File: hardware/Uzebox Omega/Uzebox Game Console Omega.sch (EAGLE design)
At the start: 81 parts, among them CON1 USBSERIALSMD, IC1 MCP1700, IC2 7805T, U5 DC IN, U6 23LC1024, X1 A/V

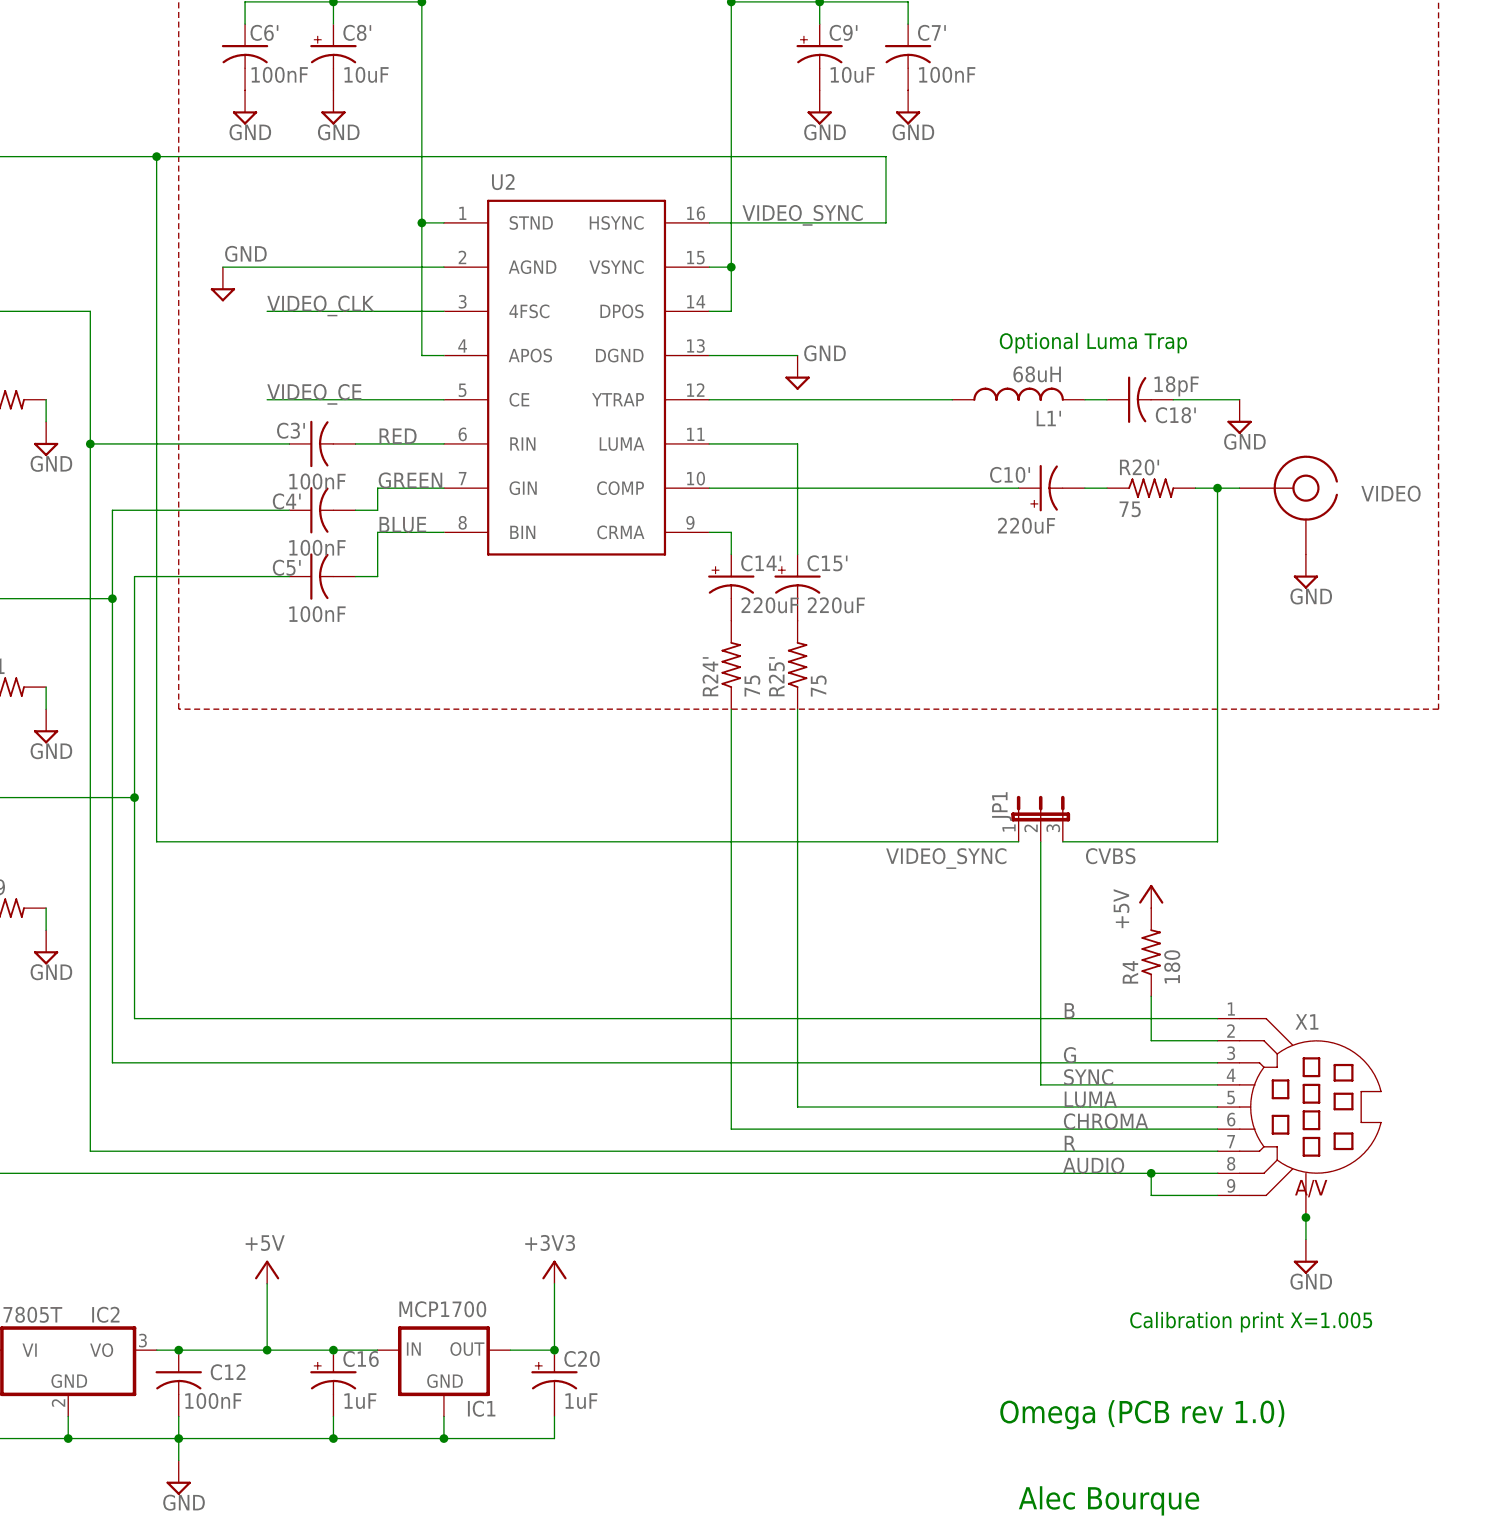
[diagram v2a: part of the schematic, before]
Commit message: Corrected pinout for Sega Megadrive cables
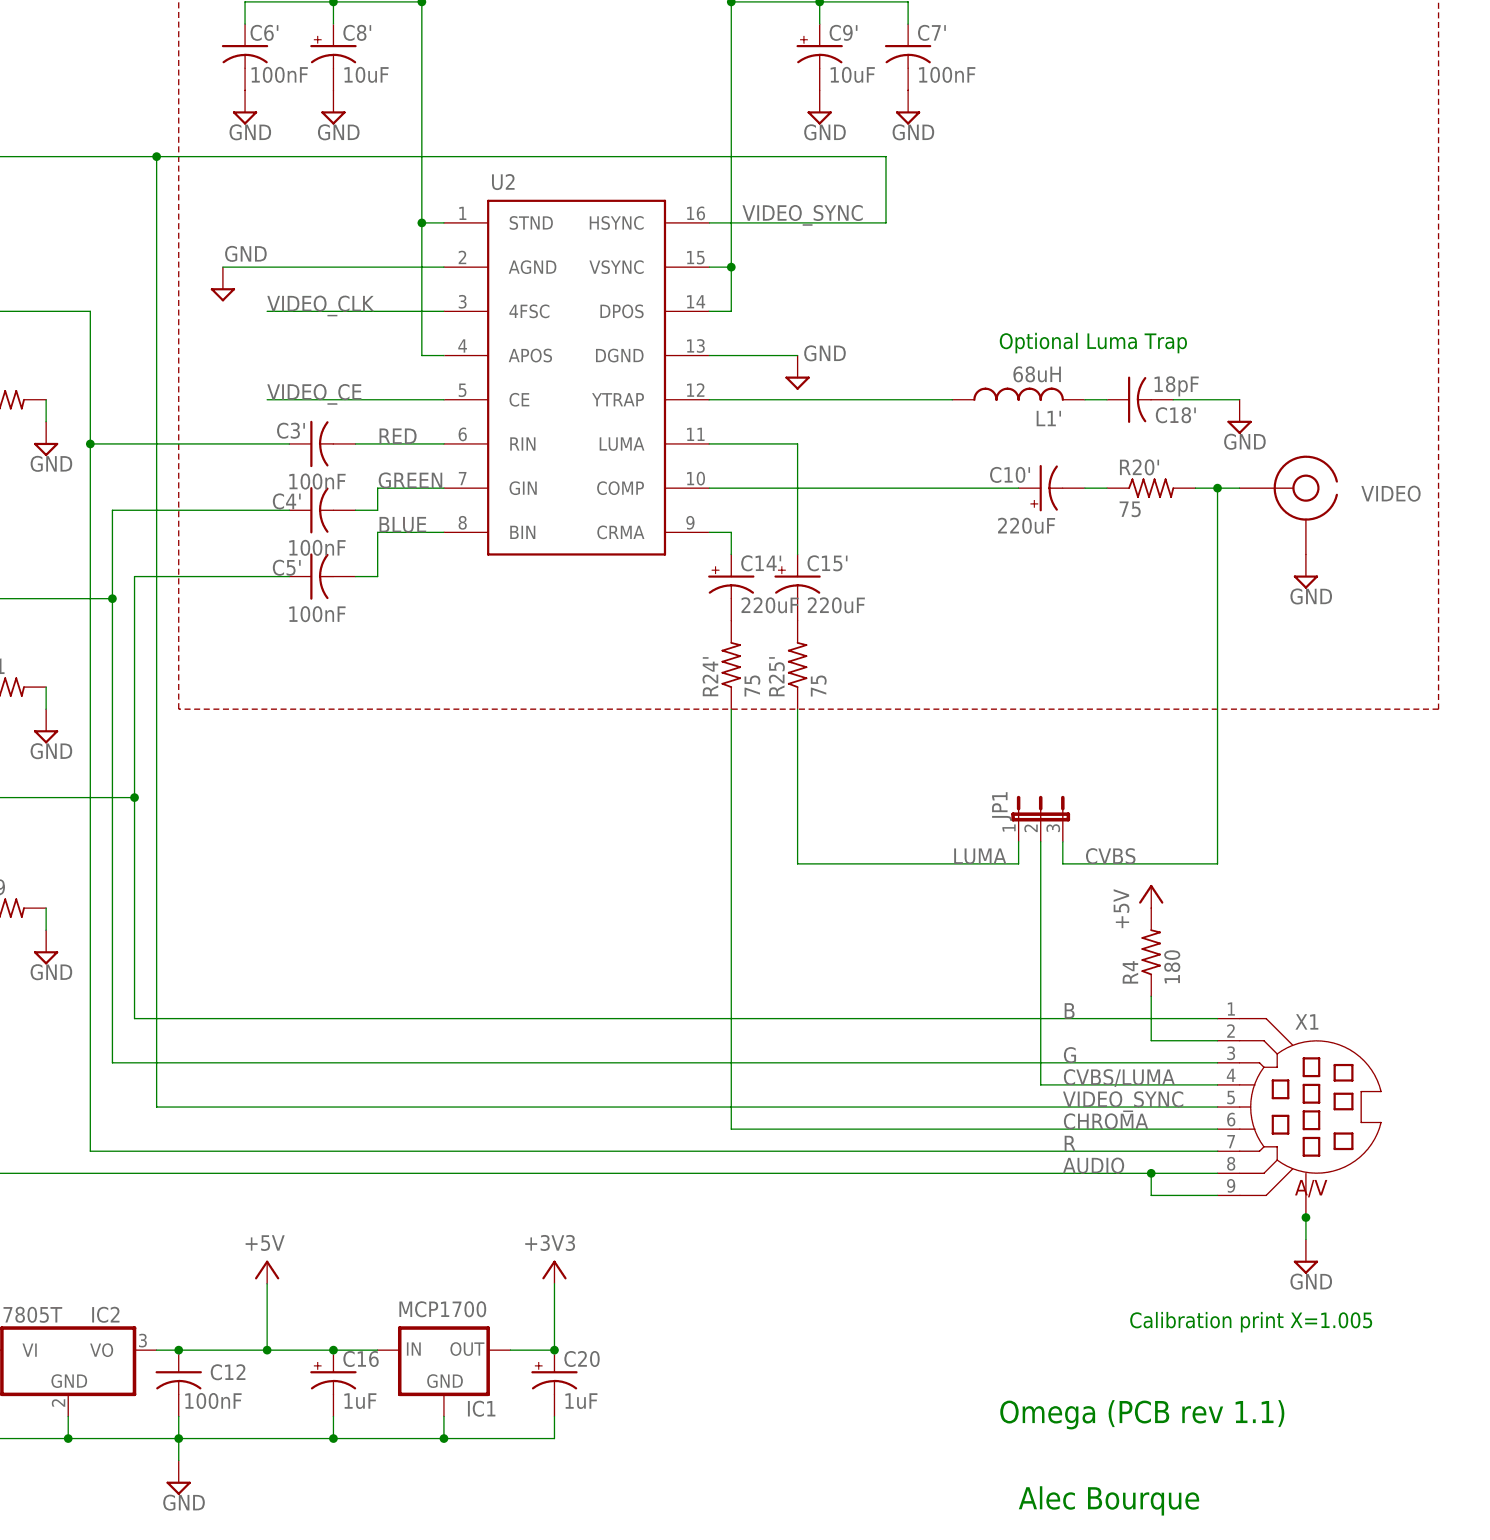
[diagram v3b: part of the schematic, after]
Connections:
- net SYNC renamed CVBS/LUMA
- net LUMA: now also JP1.1; no longer X1.5
- net VIDEO_SYNC: now also X1.5; no longer JP1.1
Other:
- note added: "Omega (PCB rev 1.1)"
- note removed: "Omega (PCB rev 1.0)"
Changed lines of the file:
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@@
 <text x="269.24" y="-30.48" size="1.778" layer="91">Calibration print X=1.005</text>
 <text x="-66.04" y="-40.64" size="1.778" layer="91">Video DAC design and SD voltage dividers contributed by Clay Cowgill.</text>
-<text x="254.254" y="-41.402" size="2.54" layer="91">Omega (PCB rev 1.0)</text>
+<text x="254.254" y="-41.402" size="2.54" layer="91">Omega (PCB rev 1.1)</text>
 <text x="165.354" y="145.542" size="1.778" layer="91">Optional Uzenet Interface</text>
 <text x="-66.04" y="-48.26" size="1.778" layer="91">Added Mini-DIN SCART connector and some cleanup by Thorsten Erdmann (Bluescreen@trektech.de)</text>
@@
 <label x="68.58" y="86.36" size="1.778" layer="95"/>
 <pinref part="MCU" gate="G$1" pin="(XCK0/T0/PCINT8)PB0"/>
-<pinref part="JP1" gate="1" pin="1"/>
 <wire x1="86.36" y1="104.14" x2="86.36" y2="86.36" width="0.1524" layer="91"/>
 <wire x1="86.36" y1="86.36" x2="68.58" y2="86.36" width="0.1524" layer="91"/>
-<label x="241.3" y="22.86" size="1.778" layer="95"/>
 <wire x1="86.36" y1="104.14" x2="157.48" y2="104.14" width="0.1524" layer="91"/>
 <wire x1="157.48" y1="104.14" x2="241.3" y2="104.14" width="0.1524" layer="91"/>
 <wire x1="241.3" y1="104.14" x2="241.3" y2="96.52" width="0.1524" layer="91"/>
-<wire x1="256.54" y1="25.4" x2="157.48" y2="25.4" width="0.1524" layer="91"/>
-<wire x1="157.48" y1="25.4" x2="157.48" y2="104.14" width="0.1524" layer="91"/>
+<wire x1="157.48" y1="-5.08" x2="157.48" y2="104.14" width="0.1524" layer="91"/>
 <junction x="157.48" y="104.14"/>
+<pinref part="X1" gate="G$1" pin="5"/>
+<wire x1="279.4" y1="-5.08" x2="157.48" y2="-5.08" width="0.1524" layer="91"/>
+<label x="261.62" y="-5.08" size="1.778" layer="95"/>
 </segment>
 <segment>
@@
 <net name="CVBS" class="0">
 <segment>
-<wire x1="281.94" y1="66.04" x2="279.4" y2="66.04" width="0.1524" layer="91"/>
 <pinref part="R20'" gate="G$1" pin="2"/>
 <pinref part="VIDEO" gate="G$1" pin="SIG"/>
+<wire x1="281.94" y1="66.04" x2="279.4" y2="66.04" width="0.1524" layer="91"/>
+<label x="264.16" y="22.86" size="1.778" layer="95"/>
 <pinref part="JP1" gate="1" pin="3"/>
 <wire x1="279.4" y1="66.04" x2="276.86" y2="66.04" width="0.1524" layer="91"/>
-<wire x1="261.62" y1="25.4" x2="279.4" y2="25.4" width="0.1524" layer="91"/>
-<wire x1="279.4" y1="25.4" x2="279.4" y2="66.04" width="0.1524" layer="91"/>
+<wire x1="261.62" y1="25.4" x2="261.62" y2="22.86" width="0.1524" layer="91"/>
+<wire x1="261.62" y1="22.86" x2="279.4" y2="22.86" width="0.1524" layer="91"/>
+<wire x1="279.4" y1="22.86" x2="279.4" y2="66.04" width="0.1524" layer="91"/>
 <junction x="279.4" y="66.04"/>
-<label x="264.16" y="22.86" size="1.778" layer="95"/>
 </segment>
 </net>
@@
 <segment>
 <pinref part="R25'" gate="G$1" pin="1"/>
-<pinref part="X1" gate="G$1" pin="5"/>
-<wire x1="279.4" y1="-5.08" x2="231.14" y2="-5.08" width="0.1524" layer="91"/>
-<wire x1="231.14" y1="-5.08" x2="231.14" y2="40.64" width="0.1524" layer="91"/>
-<label x="261.62" y="-5.08" size="1.778" layer="95"/>
+<wire x1="231.14" y1="22.86" x2="231.14" y2="40.64" width="0.1524" layer="91"/>
+<pinref part="JP1" gate="1" pin="1"/>
+<wire x1="256.54" y1="22.86" x2="231.14" y2="22.86" width="0.1524" layer="91"/>
+<wire x1="256.54" y1="25.4" x2="256.54" y2="22.86" width="0.1524" layer="91"/>
+<label x="248.92" y="22.86" size="1.778" layer="95"/>
 </segment>
 </net>
@@
 </segment>
 </net>
-<net name="SYNC" class="0">
+<net name="N$3" class="0">
+<segment>
+<wire x1="271.78" y1="149.86" x2="259.08" y2="149.86" width="0.1524" layer="91"/>
+<wire x1="259.08" y1="149.86" x2="259.08" y2="152.4" width="0.1524" layer="91"/>
+<pinref part="SJ5" gate="1" pin="2"/>
+<wire x1="259.08" y1="152.4" x2="256.54" y2="152.4" width="0.1524" layer="91"/>
+<pinref part="CON1" gate="G$1" pin="TXO"/>
+</segment>
+</net>
+<net name="N$4" class="0">
+<segment>
+<pinref part="CON1" gate="G$1" pin="RXI"/>
+<pinref part="SJ6" gate="1" pin="2"/>
+<wire x1="271.78" y1="147.32" x2="259.08" y2="147.32" width="0.1524" layer="91"/>
+<wire x1="259.08" y1="147.32" x2="259.08" y2="144.78" width="0.1524" layer="91"/>
+<wire x1="259.08" y1="144.78" x2="256.54" y2="144.78" width="0.1524" layer="91"/>
+</segment>
+</net>
+<net name="N$5" class="0">
+<segment>
+<pinref part="LED2" gate="G$1" pin="DOUT"/>
+<pinref part="LED" gate="G$1" pin="2"/>
+<wire x1="99.06" y1="7.62" x2="106.68" y2="7.62" width="0.1524" layer="91"/>
+</segment>
+</net>
+<net name="CVBS/LUMA" class="0">
 <segment>
 <pinref part="X1" gate="G$1" pin="4"/>
@@
 </segment>
 </net>
-<net name="N$3" class="0">
-<segment>
-<wire x1="271.78" y1="149.86" x2="259.08" y2="149.86" width="0.1524" layer="91"/>
-<wire x1="259.08" y1="149.86" x2="259.08" y2="152.4" width="0.1524" layer="91"/>
-<pinref part="SJ5" gate="1" pin="2"/>
-<wire x1="259.08" y1="152.4" x2="256.54" y2="152.4" width="0.1524" layer="91"/>
-<pinref part="CON1" gate="G$1" pin="TXO"/>
-</segment>
-</net>
-<net name="N$4" class="0">
-<segment>
-<pinref part="CON1" gate="G$1" pin="RXI"/>
-<pinref part="SJ6" gate="1" pin="2"/>
-<wire x1="271.78" y1="147.32" x2="259.08" y2="147.32" width="0.1524" layer="91"/>
-<wire x1="259.08" y1="147.32" x2="259.08" y2="144.78" width="0.1524" layer="91"/>
-<wire x1="259.08" y1="144.78" x2="256.54" y2="144.78" width="0.1524" layer="91"/>
-</segment>
-</net>
-<net name="N$5" class="0">
-<segment>
-<pinref part="LED2" gate="G$1" pin="DOUT"/>
-<pinref part="LED" gate="G$1" pin="2"/>
-<wire x1="99.06" y1="7.62" x2="106.68" y2="7.62" width="0.1524" layer="91"/>
-</segment>
-</net>
